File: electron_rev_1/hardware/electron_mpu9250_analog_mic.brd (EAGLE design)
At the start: 21.2 x 46.2 mm, 33 parts, among them IC2 S25FL128SAGNFI011, IC4 MIC_I2S_SPH0645, U1 MPU-9250, U2 Value, U3 OPA322AIDBVT

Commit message: cosmetic changes
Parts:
- moved C8 1.64 mm to (11.4, 32.2)
- moved R1 1.64 mm to (5.95, 26.1)
- moved U1 1.64 mm to (10.2, 27.6)
- moved R15 1.64 mm to (6.59, 8.93)
- moved U2 1.64 mm to (14.8, 10.3)
- moved C6 1.64 mm to (14.5, 3.54)
- moved R10 1.64 mm to (14.5, 1.37)
- moved R5 1.64 mm to (8.94, 5.43)
- moved C5 1.64 mm to (6.41, 2.03)
- moved IC4 1.64 mm to (10.1, 2.14)
- moved R11 1.64 mm to (4.44, 4.71)
- moved C2 1.64 mm to (6.42, 34.4)
- moved C3 1.64 mm to (14.0, 28.8)
- moved C4 1.64 mm to (15.1, 36.5)
- moved C7 1.64 mm to (15.1, 38.6)
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
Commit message: passing drc
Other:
- board size 21.2 x 46.2 mm -> 21.7 x 47.1 mm
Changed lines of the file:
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@@
 <board>
 <plain>
-<wire x1="0.02" y1="-0.04" x2="21.12" y2="0.03" width="0" layer="20"/>
-<wire x1="21.12" y1="0.03" x2="21.04" y2="46.16" width="0" layer="20"/>
-<wire x1="21.04" y1="46.16" x2="-0.06" y2="46.16" width="0" layer="20"/>
-<wire x1="-0.06" y1="46.16" x2="0.02" y2="-0.04" width="0" layer="20"/>
+<wire x1="-0.45" y1="-0.41" x2="21.25" y2="-0.41" width="0" layer="20"/>
+<wire x1="21.25" y1="-0.41" x2="21.25" y2="46.7" width="0" layer="20"/>
+<wire x1="21.25" y1="46.7" x2="-0.45" y2="46.7" width="0" layer="20"/>
+<wire x1="-0.45" y1="46.7" x2="-0.45" y2="-0.41" width="0" layer="20"/>
 <text x="13.92" y="44.68" size="0.52" layer="26" font="vector" ratio="12">N. Klugman
 M. Podolsky</text>
@@
 <via x="2.99" y="25.72" extent="1-16" drill="0.2"/>
 <via x="9.75" y="27.23" extent="1-16" drill="0.2"/>
-<wire x1="10.805" y1="25.295" x2="10.81" y2="25.29" width="0.254" layer="1"/>
 <wire x1="9.75" y1="27.23" x2="9.83" y2="27.23" width="0.2032" layer="1"/>
 <wire x1="9.83" y1="27.23" x2="10.16" y2="27.56" width="0.2032" layer="1"/>
@@
 <wire x1="9.16" y1="2.69" x2="6.42" y2="2.69" width="0.508" layer="1"/>
 <wire x1="6.42" y1="2.69" x2="6.41" y2="2.68" width="0.2" layer="1"/>
-<wire x1="10.86" y1="11.29" x2="13.6216" y2="11.29" width="0.508" layer="1"/>
+<wire x1="10.86" y1="11.29" x2="13.48" y2="11.27" width="0.508" layer="1"/>
+<wire x1="13.48" y1="11.27" x2="13.6216" y2="11.29" width="0.508" layer="1"/>
 <wire x1="10.86" y1="11.29" x2="10.86" y2="11.55" width="0.254" layer="1"/>
 <wire x1="10.86" y1="11.55" x2="10.96" y2="11.55" width="0.254" layer="1"/>
 <wire x1="10.96" y1="11.55" x2="10.96" y2="9.02" width="0.508" layer="1"/>
-<wire x1="13.6216" y1="11.29" x2="13.39" y2="11.29" width="0.254" layer="1"/>
-<wire x1="13.39" y1="19.27" x2="13.73" y2="19.61" width="0.508" layer="1"/>
+<wire x1="13.48" y1="19.25" x2="13.73" y2="19.61" width="0.508" layer="1"/>
 <wire x1="13.73" y1="19.61" x2="14.542" y2="19.61" width="0.508" layer="1"/>
 <wire x1="14.542" y1="19.61" x2="14.55" y2="19.602" width="0.254" layer="1"/>
-<wire x1="13.39" y1="11.29" x2="13.39" y2="19.27" width="0.508" layer="1"/>
+<wire x1="13.48" y1="11.27" x2="13.48" y2="19.25" width="0.508" layer="1"/>
 <wire x1="14.75" y1="21.39" x2="16.82" y2="23.46" width="0.508" layer="16"/>
 <wire x1="14.75" y1="21.39" x2="14.68" y2="21.39" width="0.254" layer="16"/>
@@
 <wire x1="16.82" y1="25.94" x2="16.82" y2="27.97" width="0.508" layer="16"/>
 <wire x1="16.8" y1="25.18" x2="16.82" y2="25.94" width="0.508" layer="16"/>
-<wire x1="9.56" y1="26.01" x2="9.57" y2="25.65" width="0.254" layer="1"/>
-<wire x1="9.57" y1="25.65" x2="9.11" y2="25.21" width="0.254" layer="1"/>
+<wire x1="9.56" y1="26.01" x2="9.56" y2="25.61" width="0.254" layer="1"/>
+<wire x1="9.56" y1="25.61" x2="9.11" y2="25.21" width="0.254" layer="1"/>
 <wire x1="7.68" y1="25.21" x2="9.11" y2="25.21" width="0.254" layer="1"/>
 <wire x1="4.16" y1="25.19" x2="5.91" y2="25.19" width="0.508" layer="1"/>
@@
 <wire x1="7.64" y1="25.24" x2="16.8" y2="25.28" width="0.508" layer="16"/>
 <wire x1="16.8" y1="25.28" x2="16.82" y2="25.11" width="0.254" layer="16"/>
-<wire x1="8.61" y1="28.56" x2="8.26" y2="28.56" width="0.254" layer="1"/>
-<wire x1="8.26" y1="28.56" x2="7.62" y2="27.91" width="0.254" layer="1"/>
-<wire x1="7.63" y1="25.2426375" x2="7.62" y2="27.91" width="0.254" layer="1"/>
+<wire x1="8.61" y1="28.56" x2="8.16" y2="28.56" width="0.254" layer="1"/>
+<wire x1="8.16" y1="28.56" x2="7.52" y2="27.91" width="0.254" layer="1"/>
+<wire x1="7.63" y1="25.2426375" x2="7.52" y2="27.91" width="0.254" layer="1"/>
 <wire x1="7.63" y1="25.2426375" x2="7.5526375" y2="25.23" width="0.254" layer="1"/>
 <wire x1="7.6326375" y1="25.24" x2="7.64" y2="25.24" width="0.2032" layer="1"/>
@@
 </signal>
 </signals>
+<errors>
+</errors>
 </board>
 </drawing>

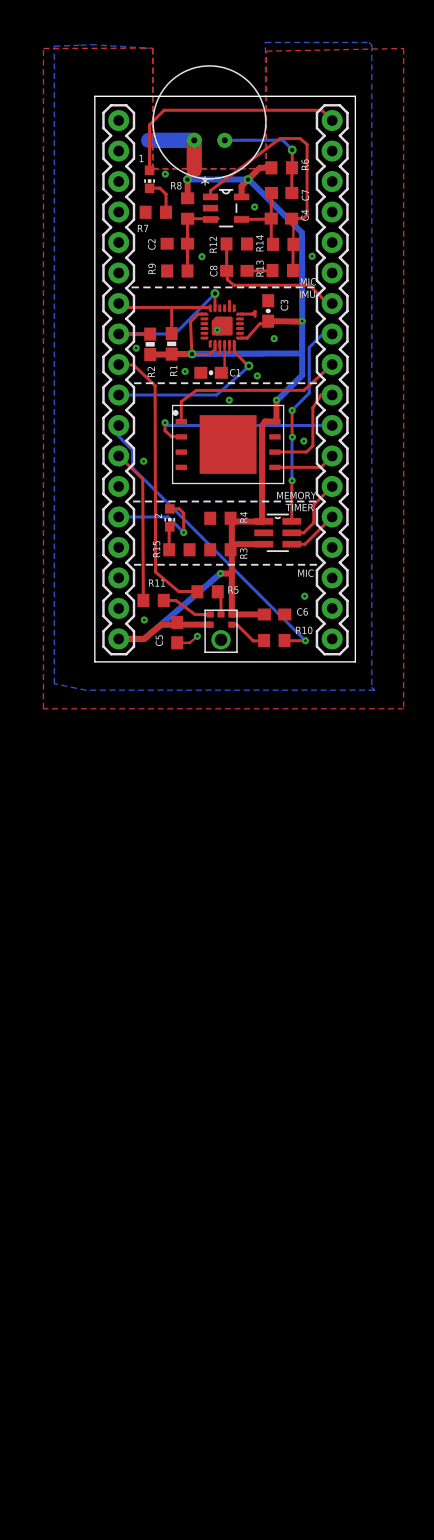
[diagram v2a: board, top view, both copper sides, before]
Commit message: fixed grid issue in schematic. added sd card. added incomplete gas sensors
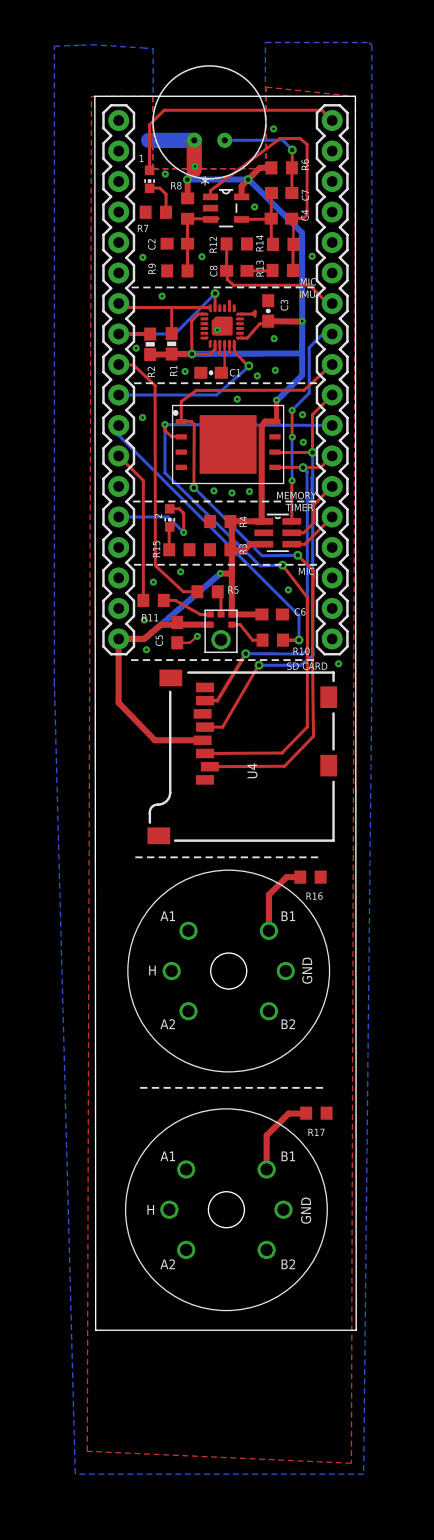
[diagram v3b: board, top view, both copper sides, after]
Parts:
- added R16, R17: 10k, resistor:R0603
- added U10, U7: GAS_SENSOR, SparkFun:MQ-3
- added U4: microSD, SparkFun:MICRO-SD-SOCKET-PP
- moved R4 0.27 mm to (10.0, 11.3), turned to 0 degrees
- moved C6 0.20 mm to (14.3, 3.54)
- moved R10 0.13 mm to (14.4, 1.40), turned to 0 degrees
- turned R3 to 0 degrees
- turned R11 to 180 degrees
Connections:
- new net G_A1: U10.A1
- new net G_A2: U7.A1
- new net G_B1: R16.2, U10.B1
- new net G_B2: R17.2, U7.B1
- new net H1: U10.HA
- new net H2: U7.HA
- net BCLK: now also U$5.8; no longer IC4.4
- net GND: now also R16.1, R17.1, R3.1, R4.1, U10.HB, U4.6, U4.CD2, U4.GND1, U4.GND2, U7.HB; no longer R3.2, R4.2
- net MISO: now also U4.3
- net MOSI: now also U4.7
- net N$2: now also IC4.1, R11.1; no longer R10.1, U$5.8
- net N$4: now also IC4.4, R10.1; no longer R11.1, U$5.7
- net SCK: now also U4.5
- net SS: now also U4.2
- net VCC: now also R3.2, R4.2, U4.4; no longer R3.1, R4.1
- net WS: now also U$5.7; no longer IC4.1
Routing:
- net SS: track 15.4 -> 58.3 mm, vias 0 -> 2
- net MISO: track 16.2 -> 56.6 mm, vias 1 -> 2
- net SCK: track 8.73 -> 40.0 mm, vias 0 -> 2
- net MOSI: track 5.16 -> 31.4 mm, vias 0 -> 2
- net BCLK: track 3.27 -> 25.5 mm, vias 0 -> 1
- net N$2: track 26.1 -> 4.18 mm, vias 1 -> 0
- net VCC: track 106.4 -> 121.1 mm
- net N$4: track 12.9 -> 3.18 mm
- net WS: track 4.25 -> 12.9 mm
- net G_B2: track 0.00 -> 6.89 mm
- net G_B1: track 0.00 -> 6.22 mm
- net GND: vias 15 -> 28
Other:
- board size 21.7 x 47.1 mm -> 21.8 x 102.8 mm
- board text added: "A1"
- board text added: "A2"
- board text added: "B1"
- board text added: "B2"
- board text added: "GND"
- board text added: "H"
- board text added: "SD CARD"

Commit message: added in that good looking Cal logo... woooooo... also did a bit more wiring for the gas sensors
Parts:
- added L1: UCB_CAL100MIL, logos:UCB_CAL_100MIL
- added SJ2: JUMPER_PAD-3-1&2_NC_BY_PASTE, SparkFun-Passives:PAD-HUMPER-3-1&2_NC_BY_PASTE_YES_SILK_FULL_BOX
- added U5, U6: +12v, SparkFun-IC-Power:TO-252
- moved R16 0.85 mm to (18.4, -18.3)
- moved U10 0.65 mm to (10.7, -25.5)
- moved R17 0.61 mm to (17.4, -37.7)
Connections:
- new net N$10: SJ2.1, U5.1, U6.1
- net GND: now also SJ2.3, U5.3, U6.3
- net H1: now also U5.2
- net H2: now also U6.2
- net VCC: now also SJ2.2
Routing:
- net N$10: track 0.00 -> 32.9 mm, vias 0 -> 2
- net H2: track 0.00 -> 25.2 mm, vias 0 -> 1
- net VCC: track 121.1 -> 134.1 mm
- net H1: track 0.00 -> 5.76 mm
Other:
- board text added: "OFF"
- board text added: "ON"

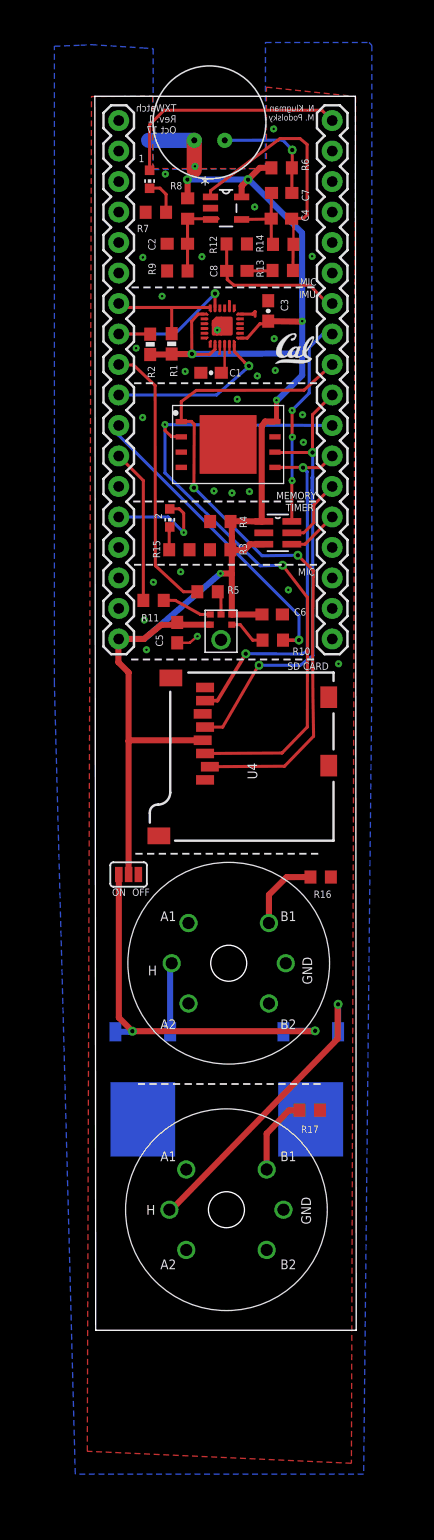
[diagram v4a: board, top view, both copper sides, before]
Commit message: generic gas sensors hooked up... haven't set up fancy CO relay thing yet. Don't know if it's worth it. Also last commit had gas sensors wired incorrectly
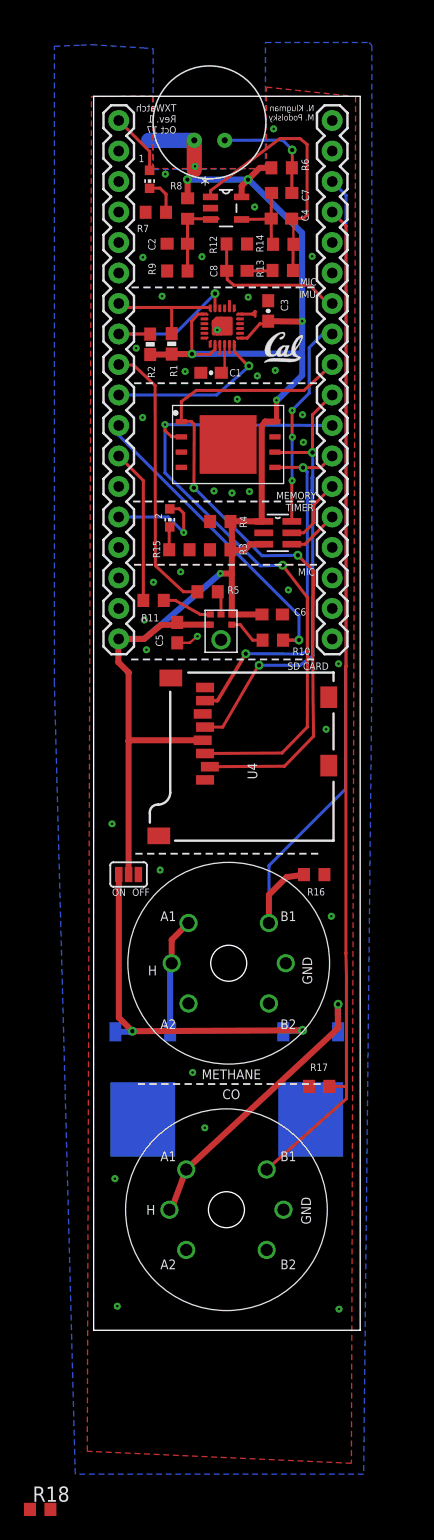
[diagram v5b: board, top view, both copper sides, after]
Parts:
- added R18: 10k, resistor:R0603
- moved R17 2.12 mm to (18.2, -35.8), turned to 0 degrees
- moved L1 0.95 mm to (13.7, 24.5)
- moved R16 0.58 mm to (17.8, -18.1)
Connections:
- removed net G_A1: U10.A1
- removed net G_A2: U7.A1
- removed net G_B1: R16.2, U10.B1
- removed net G_B2: R17.2, U7.B1
- net B0: no longer 1.A
- net B2: now also R16.2, U10.B1
- net B3: now also R17.2, U7.B1
- net C0: now also 1.A
- net H1: now also U10.A1
- net H2: now also U7.A1
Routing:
- net B3: track 0.00 -> 84.7 mm
- net B2: track 0.00 -> 70.8 mm
- net B0: track 19.9 -> 0.00 mm
- net G_B2: track 6.90 -> 0.00 mm
- net G_B1: track 6.42 -> 0.00 mm
- net C0: track 0.00 -> 5.20 mm
- net H1: track 5.76 -> 9.69 mm
- net N$10: track 32.9 -> 30.9 mm
- net GND: vias 28 -> 37
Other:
- board size 21.8 x 102.8 mm -> 22.2 x 102.8 mm
- board text added: "CO"
- board text added: "METHANE"

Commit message: gas sensors powered from battery now
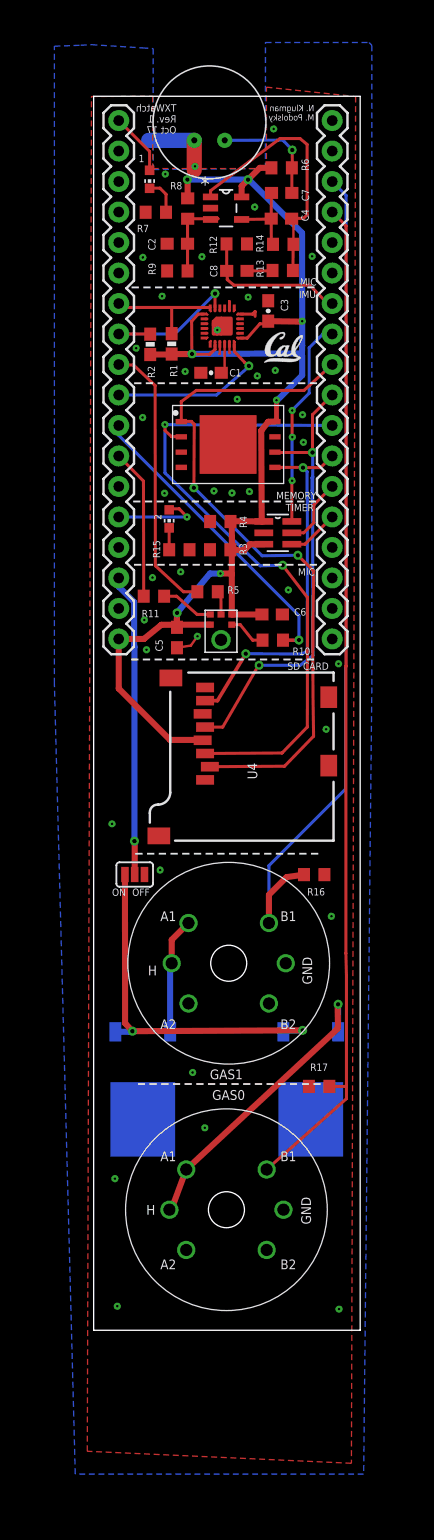
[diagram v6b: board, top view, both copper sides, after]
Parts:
- removed R18: 10k, resistor:R0603
- moved SJ2 0.51 mm to (2.87, -18.1)
- moved C5 0.41 mm to (6.39, 1.62)
- moved R11 0.35 mm to (4.47, 5.06)
- moved 2 0.09 mm to (5.74, 11.5)
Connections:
- net VBAT: now also SJ2.2
- net VCC: no longer SJ2.2
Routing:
- net VBAT: track 0.00 -> 25.3 mm, vias 0 -> 1
- net VCC: track 134.1 -> 116.3 mm, vias 6 -> 7
- net D7: track 8.90 -> 7.54 mm
- net GND: track 13.3 -> 13.5 mm, vias 37 -> 38
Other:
- board text added: "GAS0"
- board text added: "GAS1"
- board text removed: "CO"
- board text removed: "METHANE"

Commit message: fixed stupid error with solder jumper...
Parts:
- removed SJ2: JUMPER_PAD-3-1&2_NC_BY_PASTE, SparkFun-Passives:PAD-HUMPER-3-1&2_NC_BY_PASTE_YES_SILK_FULL_BOX
- added SJ1: (no value), jumper:SJ
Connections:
- net GND: no longer SJ2.3
- net N$10: now also SJ1.1; no longer SJ2.1
- net VBAT: now also SJ1.2; no longer SJ2.2
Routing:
- net N$10: track 30.7 -> 30.1 mm
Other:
- board text removed: "OFF"
- board text removed: "ON"
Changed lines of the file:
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@@
 <text x="3.97" y="-26.52" size="0.8128" layer="25" font="vector" ratio="12">H</text>
 <text x="15.59" y="-1.07" size="0.6096" layer="25" font="vector" ratio="12">SD CARD</text>
-<text x="2.66" y="-19.9" size="0.6096" layer="25" font="vector" ratio="12">OFF</text>
-<text x="0.98" y="-19.9" size="0.6096" layer="25" font="vector" ratio="12">ON</text>
 <text x="9.32" y="-36.89" size="0.8128" layer="25" font="vector" ratio="12">GAS0</text>
 <text x="9.13" y="-35.17" size="0.8128" layer="25" font="vector" ratio="12">GAS1</text>
@@
 <attribute name="VALUE" x="22.61" y="-33.48" size="1.27" layer="28" rot="MR270"/>
 </element>
-<element name="SJ2" library="SparkFun-Passives" package="PAD-HUMPER-3-1&amp;2_NC_BY_PASTE_YES_SILK_FULL_BOX" value="JUMPER_PAD-3-1&amp;2_NC_BY_PASTE" x="2.87" y="-18.12" smashed="yes">
-<attribute name="VALUE" x="2.7699" y="-18.12" size="0.02" layer="27"/>
-<attribute name="VALUE" x="1.6" y="-20.025" size="0.4064" layer="27"/>
-</element>
 <element name="L1" library="logos" package="UCB_CAL_100MIL" value="UCB_CAL100MIL" x="13.66" y="24.52"/>
+<element name="SJ1" library="jumper" library_urn="urn:adsk.eagle:library:252" package="SJ" package3d_urn="urn:adsk.eagle:package:15471/1" value="" x="2.87" y="-18.37" smashed="yes" rot="R90">
+<attribute name="VALUE" x="2.87" y="-17.9699" size="0.02" layer="27" rot="R90"/>
+</element>
 </elements>
 <signals>
@@
 <contactref element="U5" pad="3"/>
 <contactref element="U6" pad="3"/>
-<contactref element="SJ2" pad="3"/>
 <via x="0.98" y="-13.9" extent="1-16" drill="0.2"/>
 <via x="4.99" y="-17.75" extent="1-16" drill="0.2"/>
@@
 <signal name="VBAT">
 <contactref element="U$5" pad="3"/>
-<contactref element="SJ2" pad="2"/>
 <wire x1="1.54" y1="6.58" x2="1.54" y2="5.8540125" width="0.508" layer="16"/>
 <wire x1="1.54" y1="5.8540125" x2="2.8227" y2="4.5713125" width="0.508" layer="16"/>
@@
 <wire x1="2.85" y1="0.8359875" x2="2.85" y2="-15.34" width="0.508" layer="16"/>
 <wire x1="2.85" y1="-15.34" x2="2.86" y2="-15.35" width="0.508" layer="16"/>
-<wire x1="2.87" y1="-18.12" x2="2.87" y2="-15.36" width="0.508" layer="1"/>
 <via x="2.85" y="-15.34" extent="1-16" drill="0.35"/>
 <wire x1="2.87" y1="-15.36" x2="2.85" y2="-15.34" width="0.508" layer="1"/>
+<contactref element="SJ1" pad="2"/>
+<wire x1="2.85" y1="-15.34" x2="2.85" y2="-17.108" width="0.508" layer="1"/>
+<wire x1="2.85" y1="-17.108" x2="2.87" y2="-17.608" width="0.508" layer="1"/>
 </signal>
 <signal name="D7">
@@
 <wire x1="13.45" y1="11.29" x2="13.6216" y2="11.29" width="0.508" layer="1"/>
 <wire x1="10.96" y1="11.55" x2="10.96" y2="10" width="0.508" layer="1"/>
-<wire x1="13.41" y1="18.85" x2="13.99" y2="19.59" width="0.508" layer="1"/>
-<wire x1="14.542" y1="19.61" x2="13.99" y2="19.59" width="0.508" layer="1"/>
+<wire x1="13.41" y1="18.85" x2="13.99" y2="19.59" width="0.4064" layer="1"/>
 <wire x1="14.542" y1="19.61" x2="14.55" y2="19.602" width="0.254" layer="1"/>
-<wire x1="13.45" y1="11.29" x2="13.41" y2="18.85" width="0.508" layer="1"/>
-<wire x1="14.75" y1="21.39" x2="16.82" y2="23.46" width="0.508" layer="16"/>
-<wire x1="14.75" y1="21.39" x2="14.68" y2="21.39" width="0.254" layer="16"/>
+<wire x1="13.45" y1="11.29" x2="13.41" y2="18.85" width="0.4064" layer="1"/>
+<wire x1="14.63" y1="21.36" x2="16.82" y2="23.46" width="0.508" layer="16"/>
+<wire x1="14.63" y1="21.36" x2="14.68" y2="21.39" width="0.254" layer="16"/>
 <via x="14.68" y="21.39" extent="1-16" drill="0.2"/>
 <wire x1="16.82" y1="25.11" x2="16.82" y2="25.94" width="0.254" layer="16"/>
@@
 <wire x1="10.96" y1="9.218" x2="10.84" y2="8.928" width="0.508" layer="1"/>
 <wire x1="11.06" y1="8.91" x2="10.97" y2="9" width="0.508" layer="1"/>
-<wire x1="14.68" y1="21.39" x2="14.68" y2="19.748" width="0.4064" layer="1"/>
-<wire x1="14.68" y1="19.748" x2="14.542" y2="19.61" width="0.4064" layer="1"/>
 <wire x1="12.47" y1="9.39" x2="13.6216" y2="9.39" width="0.508" layer="1"/>
 <wire x1="12.01" y1="8.9" x2="12.47" y2="9.39" width="0.508" layer="1"/>
@@
 <via x="6.39544375" y="3.672365625" extent="1-16" drill="0.35"/>
 <wire x1="6.39" y1="2.47" x2="6.38" y2="3.126921875" width="0.508" layer="1"/>
-<wire x1="14.68" y1="19.748" x2="14.68" y2="19.602" width="0" layer="19" extent="1-1"/>
+<wire x1="13.99" y1="19.59" x2="14.522" y2="19.59" width="0.4064" layer="1"/>
+<wire x1="14.522" y1="19.59" x2="14.542" y2="19.61" width="0.4064" layer="1"/>
+<wire x1="14.68" y1="21.39" x2="14.68" y2="19.602" width="0.4064" layer="1"/>
+<wire x1="14.55" y1="19.602" x2="14.68" y2="19.602" width="0.4064" layer="1"/>
 </signal>
 <signal name="SCL_1">
@@
 <via x="19.81" y="-28.93" extent="1-16" drill="0.35"/>
 <wire x1="5.91" y1="-46.06" x2="5.76" y2="-46.04" width="0.508" layer="1"/>
-<wire x1="19.8" y1="-30.7" x2="19.77" y2="-29.02" width="0.508" layer="1"/>
+<wire x1="19.76" y1="-29.93" x2="19.77" y2="-29.02" width="0.508" layer="1"/>
 <wire x1="19.77" y1="-29.02" x2="19.81" y2="-28.93" width="0.508" layer="1"/>
 <contactref element="U7" pad="A1"/>
-<wire x1="19.75" y1="-30.99" x2="7.16" y2="-42.69" width="0.508" layer="1"/>
-<wire x1="19.75" y1="-30.99" x2="19.8" y2="-30.7" width="0.508" layer="1"/>
+<wire x1="19.77" y1="-30.22" x2="7.16" y2="-42.69" width="0.508" layer="1"/>
+<wire x1="19.77" y1="-30.22" x2="19.76" y2="-29.93" width="0.508" layer="1"/>
 <wire x1="7.16" y1="-42.69" x2="5.91" y2="-46.06" width="0.508" layer="1"/>
 </signal>
@@
 <wire x1="16.86" y1="-31.1" x2="15.33" y2="-31.14" width="0.508" layer="16"/>
 <wire x1="15.33" y1="-31.14" x2="15.25" y2="-31.22" width="0.508" layer="16"/>
-<contactref element="SJ2" pad="1"/>
-<wire x1="2.0572" y1="-18.12" x2="2.07" y2="-30.5072" width="0.508" layer="1"/>
-<wire x1="2.07" y1="-30.5072" x2="2.68" y2="-31.17" width="0.508" layer="1"/>
+<wire x1="2.64" y1="-18.8472" x2="2.68" y2="-31.17" width="0.508" layer="1"/>
+<contactref element="SJ1" pad="1"/>
+<wire x1="2.87" y1="-19.132" x2="2.87" y2="-19.0772" width="0.4064" layer="1"/>
+<wire x1="2.87" y1="-19.0772" x2="2.64" y2="-18.8472" width="0.4064" layer="1"/>
 </signal>
 </signals>
